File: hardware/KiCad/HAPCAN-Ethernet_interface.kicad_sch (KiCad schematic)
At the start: 13 parts, among them CON1 Connectors CAN bus, IC1 MCP16301HT, U1 HLK-7628N

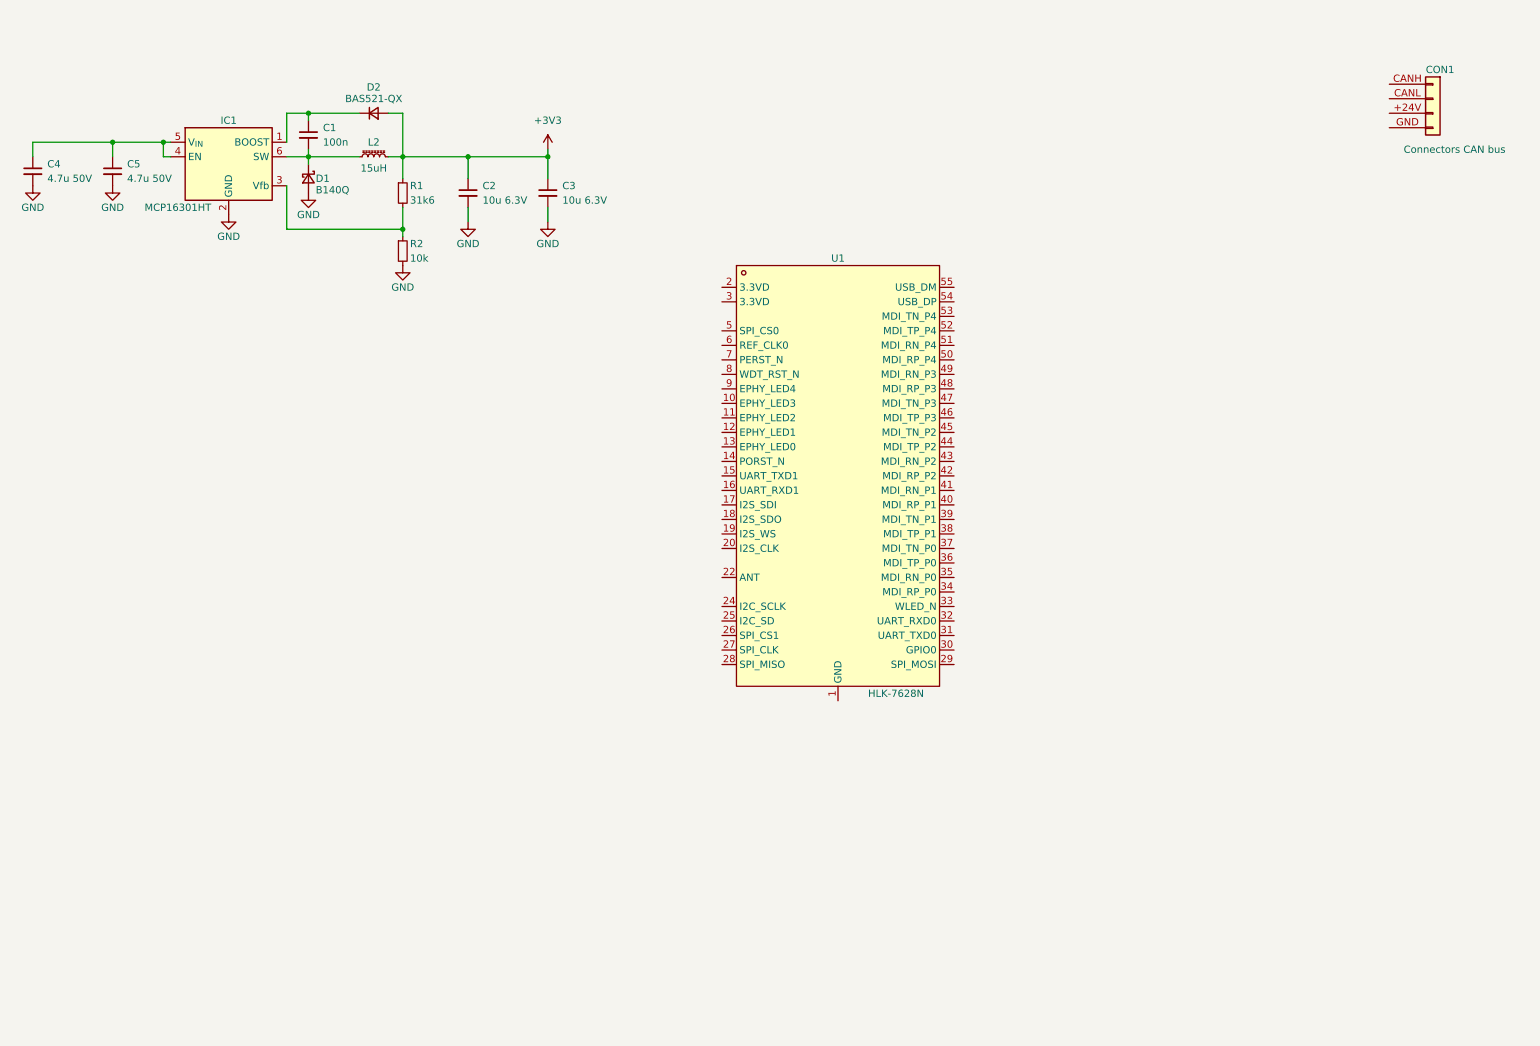
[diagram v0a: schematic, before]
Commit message: Made some progress in schematic, preliminary component placement on board
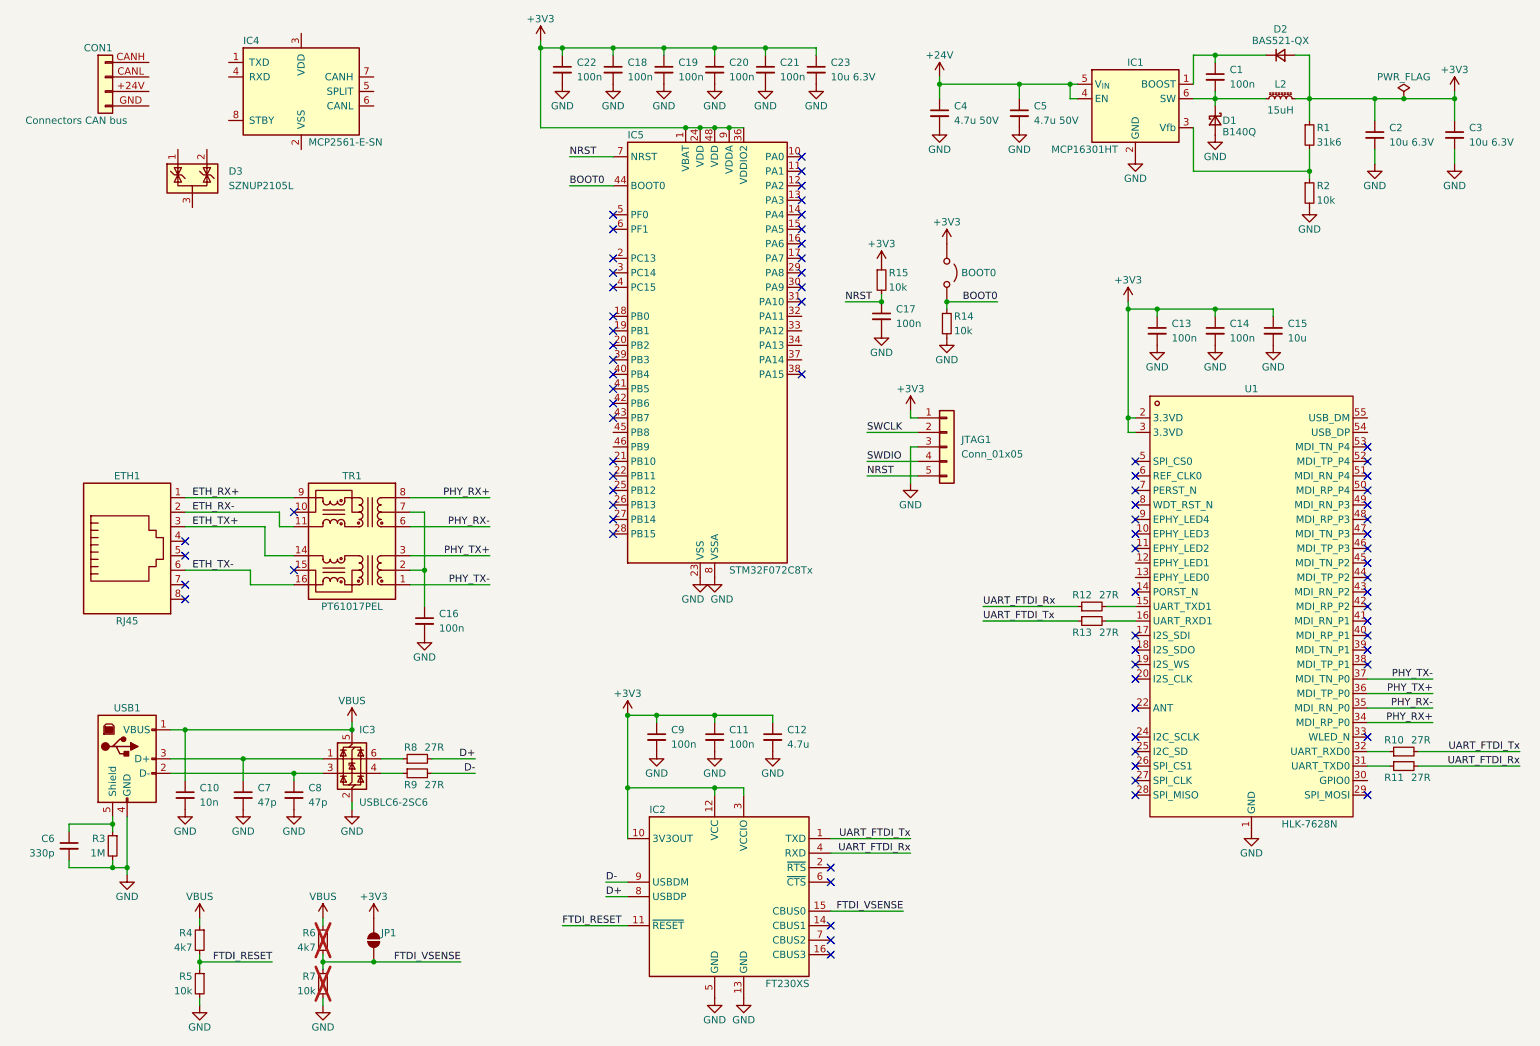
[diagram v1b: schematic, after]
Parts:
- added BOOT0: Jumper_2_Open, Connector_PinHeader_2.54mm:PinHeader_1x02_P2.54mm_Vertical, symbol Jumper:Jumper_2_Open
- added C10: 10n, Capacitor_SMD:C_0603_1608Metric_Pad1.08x0.95mm_HandSolder, symbol Device:C_Small
- added C11, C13, C14, C16, C17, C18, C19, C20, C21, C22, C9: 100n, Capacitor_SMD:C_0603_1608Metric_Pad1.08x0.95mm_HandSolder, symbol Device:C_Small
- added C12: 4.7u, Capacitor_SMD:C_1206_3216Metric_Pad1.33x1.80mm_HandSolder, symbol Device:C_Small
- added C15: 10u, Capacitor_SMD:C_1206_3216Metric_Pad1.33x1.80mm_HandSolder, symbol Device:C_Small
- added C23: 10u 6.3V, Capacitor_SMD:C_1206_3216Metric_Pad1.33x1.80mm_HandSolder, symbol Device:C_Small
- added C6: 330p, Capacitor_SMD:C_0603_1608Metric_Pad1.08x0.95mm_HandSolder, symbol Device:C_Small
- added C7, C8: 47p, Capacitor_SMD:C_0603_1608Metric_Pad1.08x0.95mm_HandSolder, symbol Device:C_Small
- added D3: SZNUP2105L, Package_TO_SOT_SMD:SOT-23, symbol Power_Protection:SZNUP2105L
- added ETH1: RJ45, ProjectLib:RJ45-PCB-SOCKET, symbol Connector:RJ45
- added IC2: FT230XS, Package_SO:SSOP-16_3.9x4.9mm_P0.635mm, symbol Interface_USB:FT230XS
- added IC3: USBLC6-2SC6, Package_TO_SOT_SMD:SOT-23-6_Handsoldering, symbol Power_Protection:USBLC6-2SC6
- added IC4: MCP2561-E-SN, Package_SO:SOIC-8_3.9x4.9mm_P1.27mm, symbol Interface_CAN_LIN:MCP2561-E-SN
- added IC5: STM32F072C8Tx, Package_QFP:LQFP-48_7x7mm_P0.5mm, symbol MCU_ST_STM32F0:STM32F072C8Tx
- added JP1: SolderJumper_2_Open, Jumper:SolderJumper-2_P1.3mm_Open_TrianglePad1.0x1.5mm, symbol Jumper:SolderJumper_2_Open
- added JTAG1: Conn_01x05, Connector_PinHeader_2.54mm:PinHeader_1x05_P2.54mm_Vertical, symbol Connector_Generic:Conn_01x05
- added R10, R11, R12, R13, R8, R9: 27R, Resistor_SMD:R_0603_1608Metric_Pad0.98x0.95mm_HandSolder, symbol Device:R_Small
- added R14, R15, R5, R7: 10k, Resistor_SMD:R_0603_1608Metric_Pad0.98x0.95mm_HandSolder, symbol Device:R_Small
- added R3: 1M, Resistor_SMD:R_0603_1608Metric_Pad0.98x0.95mm_HandSolder, symbol Device:R_Small
- added R4, R6: 4k7, Resistor_SMD:R_0603_1608Metric_Pad0.98x0.95mm_HandSolder, symbol Device:R_Small
- added TR1: PT61017PEL, Transformer_SMD:Transformer_Ethernet_Bourns_PT61017PEL, symbol ProjectLib:PT61017PEL
- added USB1: https://www.aliexpress.com/item/4000926155068.html, Connector_PinHeader_2.54mm:PinHeader_1x05_P2.54mm_Vertical, symbol Connector:USB_B
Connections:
- net +3V3: now also U1.2 (3.3VD), U1.3 (3.3VD), BOOT0.1 (A), C11.1, C12.1, C13.1, C14.1, C15.1, C18.1, C19.1, C20.1, C21.1, C22.1, C23.1, C9.1, IC2.10 (3V3OUT), IC2.12 (VCC), IC2.3 (VCCIO), IC5.1 (VBAT), IC5.24 (VDD), IC5.36 (VDDIO2), IC5.48 (VDD), IC5.9 (VDDA), JP1.2 (B), JTAG1.1 (Pin_1), R15.1
- net GND: now also U1.1 (GND), U1.21 (GND), U1.23 (GND), U1.4 (GND), U1.56 (GND), C10.2, C11.2, C12.2, C13.2, C14.2, C15.2, C16.2, C17.2, C18.2, C19.2, C20.2, C21.2, C22.2, C23.2, C6.2, C7.2, C8.2, C9.2, IC2.13 (GND), IC2.5 (GND), IC3.2 (GND), IC5.23 (VSS), IC5.35 (VSS), IC5.47 (VSS), IC5.8 (VSSA), JTAG1.3 (Pin_3), R14.2, R3.2, R5.2, R7.2, USB1.4 (GND)
- net at U1.15 (UART_TXD1): now also R12.2
- net at U1.16 (UART_RXD1): now also R13.2
- net at U1.31 (UART_TXD0): now also R11.1
- net at U1.32 (UART_RXD0): now also R10.1
- net PHY_RX+: now reaches U1.34 (MDI_RP_P0)
- net PHY_RX+: now also TR1.8 (RD-)
- net PHY_RX-: now reaches U1.35 (MDI_RN_P0)
- net PHY_RX-: now also TR1.6 (RD+)
- net PHY_TX+: now reaches U1.36 (MDI_TP_P0)
- net PHY_TX+: now also TR1.3 (TD-)
- net PHY_TX-: now reaches U1.37 (MDI_TN_P0)
- net PHY_TX-: now also TR1.1 (TD+)
- net +24V: now reaches C4.1, C5.1, IC1.4 (EN), IC1.5 (V_{IN})
- new net: C16.1, TR1.2 (C_TD), TR1.7 (C_RD)
- new net: C7.1, IC3.1 (I/O1), USB1.3 (D+)
- new net: C8.1, IC3.3 (I/O2), USB1.2 (D-)
- new net: IC3.4 (I/O2), R9.1
- new net: IC3.6 (I/O1), R8.1
- new net: C6.1, R3.1, USB1.5 (Shield)
- new net BOOT0: BOOT0.2 (B), IC5.44 (BOOT0), R14.1
- new net D+: IC2.8 (USBDP), R8.2
- new net D-: IC2.9 (USBDM), R9.2
- new net ETH_RX+: ETH1.1, TR1.9 (RX-)
- new net ETH_RX-: ETH1.2, TR1.11 (RX+)
- new net ETH_TX+: ETH1.3, TR1.14 (TX-)
- new net ETH_TX-: ETH1.6, TR1.16 (TX+)
- new net FTDI_RESET: IC2.11 (~{RESET}), R4.2, R5.1
- new net FTDI_VSENSE: IC2.15 (CBUS0), JP1.1 (A), R6.2, R7.1
- new net NRST: C17.1, IC5.7 (NRST), JTAG1.5 (Pin_5), R15.2
- new net SWCLK: JTAG1.2 (Pin_2)
- new net SWDIO: JTAG1.4 (Pin_4)
- new net UART_FTDI_Rx: IC2.4 (RXD), R11.2, R12.1
- new net UART_FTDI_Tx: IC2.1 (TXD), R10.2, R13.1
- new net VBUS: C10.1, IC3.5 (VBUS), R4.1, R6.1, USB1.1 (VBUS)
- no-connect marks 0 -> 78
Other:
- moved on the sheet: C1, C2, C3, C4, C5, CON1, D1, D2, IC1, L2, R1, R2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

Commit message: Finished schematic, but needs cleanup. Started component placement on board.
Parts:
- added C1, C15, C2, C21, C23, C24, C6, C7: 100n, Capacitor_SMD:C_0603_1608Metric_Pad1.08x0.95mm_HandSolder, symbol Device:C_Small
- added C16, C8: 10u 16V, Capacitor_SMD:C_1210_3225Metric_Pad1.33x2.70mm_HandSolder, symbol Device:C_Small
- added C17: 10u 10V, Capacitor_SMD:C_1210_3225Metric_Pad1.33x2.70mm_HandSolder, symbol Device:C_Small
- added C18: 22u 10V, Capacitor_SMD:C_1210_3225Metric_Pad1.33x2.70mm_HandSolder, symbol Device:C_Small
- added C20: 10n, Capacitor_SMD:C_0603_1608Metric_Pad1.08x0.95mm_HandSolder, symbol Device:C_Small
- added C22: 10u 6.3V, Capacitor_SMD:C_1206_3216Metric_Pad1.33x1.80mm_HandSolder, symbol Device:C_Small
- added C3: 10u 10V, Capacitor_SMD:C_1206_3216Metric_Pad1.33x1.80mm_HandSolder, symbol Device:C_Small
- added C4, C5: 4.7u 50V, Capacitor_SMD:C_1210_3225Metric_Pad1.33x2.70mm_HandSolder, symbol Device:C_Small
- added D1: US1D, Diode_SMD:D_SMA_Handsoldering, symbol Diode:US1D
- added FB1, FB2: 1k@100MHz, Inductor_SMD:L_0805_2012Metric_Pad1.15x1.40mm_HandSolder, symbol Device:FerriteBead_Small
- added IC1: LMR51430Y, Package_TO_SOT_SMD:SOT-23-6, symbol Regulator_Switching:LMR51430
- added IC3: TLV62568DRL, Package_TO_SOT_SMD:SOT-563, symbol Regulator_Switching:TLV62568DRL
- added IC5: MCP3422A0-E/MS, Package_SO:MSOP-8_3x3mm_P0.65mm, symbol Analog_ADC:MCP3422Axx-xMS
- added L1: 3.3uH, ProjectLib:SPM7054VT, symbol Device:L_Ferrite_Small
- added L2: 1uH, ProjectLib:SPM7054VT, symbol Device:L_Ferrite_Small
- added NT1, NT2, NT3, NT4: NetTie_2, NetTie:NetTie-2_SMD_Pad0.5mm, symbol Device:NetTie_2
- added R1: 200k, Resistor_SMD:R_0603_1608Metric_Pad0.98x0.95mm_HandSolder, symbol Device:R_Small
- added R10, R4, R8, R9: 22k, Resistor_SMD:R_0603_1608Metric_Pad0.98x0.95mm_HandSolder, symbol Device:R_Small
- added R13, R14: 10k, Resistor_SMD:R_0603_1608Metric_Pad0.98x0.95mm_HandSolder, symbol Device:R_Small
- added R2: 27k, Resistor_SMD:R_0603_1608Metric_Pad0.98x0.95mm_HandSolder, symbol Device:R_Small
- added R3: 100k, Resistor_SMD:R_0603_1608Metric_Pad0.98x0.95mm_HandSolder, symbol Device:R_Small
- added R7: 330k, Resistor_SMD:R_0603_1608Metric_Pad0.98x0.95mm_HandSolder, symbol Device:R_Small
- added TVS1: P6SMB33CA, Diode_SMD:D_SMB_Handsoldering, symbol Device:D_TVS_Small
- renumbered BOOT0 to BOOT1, C18 to C10, C19 to C11, C20 to C12, C21 to C13, C23 to C14, C17 to C19, C13 to C25, C14 to C26, C15 to C27, C16 to C28, C9 to C29, C11 to C30, C12 to C31, C10 to C32, C7 to C33, C8 to C34, C6 to C35, C1 to C36, C4 to C37, C5 to C38, C2 to C39, C3 to C40, C22 to C9, D1 to D3, IC4 to IC2, IC5 to IC4, IC3 to IC6, IC2 to IC7, IC1 to IC8, L2 to L3, R12 to R11, R13 to R12, R10 to R15, R11 to R16, R8 to R17, R9 to R18, R3 to R19, R4 to R20, R6 to R21, R5 to R22, R7 to R23, R1 to R24, R2 to R25, R15 to R5, R14 to R6, D3 to TVS2
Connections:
- net +24V: now also C4.1, C5.1, C6.1, FB1.2, IC1.3 (VIN), IC1.5 (EN), NT1.1
- net +3V3: now also C17.1, C18.1, C20.1, C21.1, C22.1, IC5.3 (V_{DD}), L2.2, NT3.1, R13.1, R14.1, R3.1
- net D+: now also R18.2; no longer R17.2
- net D-: now also R17.2; no longer R18.2
- net GND: now also IC2.2 (VSS), IC2.8 (STBY), C16.2, C17.2, C18.2, C2.2, C20.2, C21.2, C22.2, C3.2, C4.2, C5.2, C6.2, C7.2, C8.2, FB2.2, IC1.1 (GND), IC3.2 (GND), IC5.6 (V_{SS}), NT2.1, NT4.1, R2.2, R4.2
- net SWCLK: now also IC4.37 (PA14)
- net SWDIO: now also IC4.34 (PA13)
- net I2C_CLK: now reaches U1.24 (I2C_SCLK)
- net I2C_CLK: now also IC5.5 (SCL), R13.2
- net I2C_SDA: now reaches U1.25 (I2C_SD)
- net I2C_SDA: now also IC5.4 (SDA), R14.2
- net CAN_USB_D+: now reaches U1.54 (USB_DP)
- net CAN_USB_D+: now also IC4.33 (PA12)
- net CAN_USB_D-: now reaches U1.55 (USB_DM)
- net CAN_USB_D-: now also IC4.32 (PA11)
- net CAN_Tx: now reaches IC2.1 (TXD)
- net CAN_Tx: now also IC4.46 (PB9)
- net +5V: now reaches IC2.3 (VDD)
- net +5V: now also C16.1, C2.1, C3.1, C7.1, C8.1, IC3.3 (VIN), IC3.5 (EN), L1.2, R1.1
- net CAN_Rx: now reaches IC2.4 (RXD)
- net CAN_Rx: now also IC4.45 (PB8)
- net CANL: now reaches IC2.6 (CANL)
- net CANL: now also CON1.CANL, TVS2.2 (K)
- net CANH: now reaches IC2.7 (CANH)
- net CANH: now also CON1.CANH, TVS2.1 (K)
- net at C33.1, USB1.3 (D+): now also IC6.3 (I/O2); no longer IC6.1 (I/O1)
- net at C34.1, USB1.2 (D-): now also IC6.1 (I/O1); no longer IC6.3 (I/O2)
- net GNDPWR: now reaches TVS2.3 (A)
- net GNDPWR: now also CON1.GND, C15.2, FB2.1, TVS1.1 (A1)
- net at CON1.+24V: now also C15.1, D1.2 (A), TVS1.2 (A2)
- new net: D1.1 (K), FB1.1
- new net: IC1.4 (FB), R1.2, R2.1
- new net: C23.2, IC5.1 (CH1+), R7.2, R8.1
- new net: C24.2, IC5.7 (CH2+), R10.1, R9.2
- new net: IC3.1 (FB), R3.2, R4.1
- new net: C1.1, IC1.6 (CB)
- new net: C1.2, IC1.2 (SW), L1.1
- new net: IC3.4 (SW), L2.1
- new net ADC_24V: NT1.2, R7.1
- new net ADC_3V3: NT3.2, R9.1
- new net ADC_GND: C23.1, IC5.2 (CH1-), NT2.2, R8.2
- new net ADC_GND2: C24.1, IC5.8 (CH2-), NT4.2, R10.2
- no-connect marks 78 -> 80
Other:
- note added: "Not used"
- title: (none) -> HAPCAN Ethernet interface
- moved on the sheet: BOOT1, C10, C11, C12, C13, C14, C19, C25, C26, C27, C28, C29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

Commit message: Did some work on board.
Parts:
- TVS2: footprint Package_TO_SOT_SMD:SOT-23 -> Package_TO_SOT_SMD:SOT-23-3
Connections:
- net CANH: now also TVS2.2 (K); no longer TVS2.1 (K)
- net CANL: now also TVS2.1 (K); no longer TVS2.2 (K)
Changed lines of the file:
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@@
 	)
 	(junction
-		(at 123.19 52.07)
+		(at 66.04 127)
 		(diameter 0)
 		(color 0 0 0 0)
 	)
 	(junction
-		(at 66.04 127)
+		(at 128.27 52.07)
+		(diameter 0)
+		(color 0 0 0 0)
+	)
+	(junction
+		(at 123.19 46.99)
 		(diameter 0)
 		(color 0 0 0 0)
@@
 	)
 	(junction
-		(at 128.27 46.99)
-		(diameter 0)
-		(color 0 0 0 0)
-	)
-	(junction
 		(at 209.55 38.1)
 		(diameter 0)
@@
 	(wire
 		(pts
-			(xy 123.19 52.07) (xy 133.35 52.07)
+			(xy 115.57 52.07) (xy 128.27 52.07)
 		)
 		(stroke
@@
 	(wire
 		(pts
-			(xy 128.27 46.99) (xy 128.27 53.34)
+			(xy 73.66 134.62) (xy 73.66 115.57)
 		)
 		(stroke
@@
 	(wire
 		(pts
-			(xy 73.66 134.62) (xy 73.66 115.57)
+			(xy 128.27 52.07) (xy 133.35 52.07)
 		)
 		(stroke
@@
 	(wire
 		(pts
-			(xy 128.27 46.99) (xy 133.35 46.99)
-		)
-		(stroke
-			(width 0)
-			(type default)
-		)
-	)
-	(wire
-		(pts
 			(xy 247.65 87.63) (xy 233.68 87.63)
 		)
@@
 	(wire
 		(pts
+			(xy 128.27 53.34) (xy 128.27 52.07)
+		)
+		(stroke
+			(width 0)
+			(type default)
+		)
+	)
+	(wire
+		(pts
 			(xy 311.15 320.04) (xy 311.15 317.5)
 		)
@@
 	(wire
 		(pts
+			(xy 123.19 46.99) (xy 133.35 46.99)
+		)
+		(stroke
+			(width 0)
+			(type default)
+		)
+	)
+	(wire
+		(pts
+			(xy 123.19 53.34) (xy 123.19 46.99)
+		)
+		(stroke
+			(width 0)
+			(type default)
+		)
+	)
+	(wire
+		(pts
 			(xy 158.75 46.99) (xy 167.64 46.99)
 		)
@@
 	(wire
 		(pts
-			(xy 123.19 52.07) (xy 123.19 53.34)
-		)
-		(stroke
-			(width 0)
-			(type default)
-		)
-	)
-	(wire
-		(pts
 			(xy 144.78 217.17) (xy 144.78 215.9)
 		)
@@
 	(wire
 		(pts
-			(xy 115.57 52.07) (xy 123.19 52.07)
-		)
-		(stroke
-			(width 0)
-			(type default)
-		)
-	)
-	(wire
-		(pts
 			(xy 388.62 30.48) (xy 388.62 27.94)
 		)
@@
 	(wire
 		(pts
-			(xy 115.57 46.99) (xy 128.27 46.99)
+			(xy 115.57 46.99) (xy 123.19 46.99)
 		)
 		(stroke
@@
 			)
 		)
-		(property "Footprint" "Package_TO_SOT_SMD:SOT-23"
+		(property "Footprint" "Package_TO_SOT_SMD:SOT-23-3"
 			(at 120.015 59.69 0)
 			(effects

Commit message: Updated schematic, finished the board routing
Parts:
- removed C26: 100n, Capacitor_SMD:C_0603_1608Metric_Pad1.08x0.95mm_HandSolder, symbol Device:C_Small
- removed C39, C40: 10u 6.3V, Capacitor_SMD:C_1206_3216Metric_Pad1.33x1.80mm_HandSolder, symbol Device:C_Small
- removed D2: BAS521-QX, Diode_SMD:D_SOD-523, symbol Device:D_Small
- removed D3: B140Q, Diode_SMD:D_SMA, symbol Device:D_Schottky_Small
- removed ETH1: RJ45, ProjectLib:RJ45-PCB-SOCKET, symbol Connector:RJ45
- removed IC3: TLV62568DRL, Package_TO_SOT_SMD:SOT-563, symbol Regulator_Switching:TLV62568DRL
- removed IC8: MCP16301HT, Package_TO_SOT_SMD:SOT-23-6, symbol Regulator_Switching:MCP16301Hx-xCH
- removed L3: 15uH, Inductor_SMD:L_Wuerth_WE-PD-Typ-M-Typ-S_Handsoldering, symbol Device:L_Ferrite_Small
- removed NT3: NetTie_2, NetTie:NetTie-2_SMD_Pad0.5mm, symbol Device:NetTie_2
- added BAT1: CR2032, ProjectLib:1074, symbol Device:Battery_Cell
- added C41: 10u 16V, Capacitor_SMD:C_1210_3225Metric_Pad1.33x2.70mm_HandSolder, symbol Device:C_Small
- added C42: 100n, Capacitor_SMD:C_0603_1608Metric_Pad1.08x0.95mm_HandSolder, symbol Device:C_Small
- added ETH1: RJ45_Shielded, Connector_RJ:RJ45_Ninigi_GE, symbol Connector:8P8C_Shielded
- added IC3: TLV62568DBV, Package_TO_SOT_SMD:SOT-23-5, symbol Regulator_Switching:TLV62568DBV
- added IC8: BQ32000, Package_SO:SOIC-8_3.9x4.9mm_P1.27mm, symbol Timer_RTC:BQ32000
- added R26: 330R, Resistor_SMD:R_0603_1608Metric_Pad0.98x0.95mm_HandSolder, symbol Device:R_Small
- added R27: 1M, Resistor_SMD:R_0603_1608Metric_Pad0.98x0.95mm_HandSolder, symbol Device:R_Small
- added T1: DMC2053UVT, Package_TO_SOT_SMD:TSOT-23-6, symbol Transistor_FET:DMC2053UVT
- added XTAL1: ECS-.327-12.5-34QCS-TR, Crystal:Crystal_SMD_EuroQuartz_EQ161-2Pin_3.2x1.5mm_HandSoldering, symbol Device:Crystal_Small
- C36: value 100n -> 1u; footprint Capacitor_SMD:C_0603_1608Metric_Pad1.08x0.95mm_HandSolder -> Capacitor_SMD:C_0805_2012Metric_Pad1.18x1.45mm_HandSolder
- C37: value 4.7u 50V -> 100n; footprint Capacitor_SMD:C_1210_3225Metric_Pad1.33x2.70mm_HandSolder -> Capacitor_SMD:C_0603_1608Metric_Pad1.08x0.95mm_HandSolder
- C38: value 4.7u 50V -> 330p; footprint Capacitor_SMD:C_1210_3225Metric_Pad1.33x2.70mm_HandSolder -> Capacitor_SMD:C_0603_1608Metric_Pad1.08x0.95mm_HandSolder
- R13, R14: value 10k -> 4k7
- R24: value 31k6 -> 47k
- R25: value 10k -> 47k
- renumbered BOOT1 to BOOT0
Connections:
- net +24V: no longer C37.1, C38.1
- net +3V3: now also C36.1, C37.1, C42.1, IC8.8 (VCC); no longer R24.1
- net +5V: now also C41.1, IC3.1 (EN), IC3.4 (VIN)
- net ETH_RX+: now also ETH1.1
- net ETH_RX-: now also ETH1.2
- net ETH_TX+: now also ETH1.3
- net ETH_TX-: now also ETH1.6
- net GND: now also C36.2, BAT1.2 (-), C41.2, C42.2, IC3.2 (GND), IC8.4 (GND), R27.2, T1.5 (S)
- net I2C_CLK: now also IC8.6 (SCL)
- net I2C_SDA: now also IC8.5 (SDA)
- net BAT_MEAS_EN: now reaches U1.30 (GPIO0)
- net BAT_MEAS_EN: now also R26.1
- net at C24.2, IC5.7 (CH2+), R10.1: now also T1.4 (D); no longer R9.2
- net at R25.1: now also R26.2, T1.1 (G); no longer R24.2
- net at R3.2, R4.1: now also IC3.5 (FB)
- net at L2.1: now also IC3.3 (SW)
- net ADC_3V3 renamed ADC_BAT
- net ADC_BAT: now also R24.1, T1.2 (S)
- new net: IC8.1 (OSCI), XTAL1.1
- new net: IC8.2 (OSCO), XTAL1.2
- new net: C38.1, ETH1.SH, R27.1
- new net: R24.2, T1.3 (G), T1.6 (D)
- new net +BATT: BAT1.1 (+), IC8.3 (VBACK), R9.2
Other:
- note added: "ADC"
- note added: "CAN bus, 24V input"
- note added: "CANable interface"
- note added: "Ethernet"
- note added: "Linux SoM"
- note added: "Power"
- note added: "RTC"
- note added: "USB console"
- note removed: "Not used"
- company: (none) -> Ondrej Kolar
- moved on the sheet: BOOT0, C1, C10, C11, C12, C13, C14, C15, C16, C17, C18, C19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
